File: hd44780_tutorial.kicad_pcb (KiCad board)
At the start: 2 copper layers, 157.2 x 83.5 mm, 33 parts, among them J1 LCD_2004_PinSocket_1x16_P2.54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, J2 UJC-HP-3-SMT-TR, SW1 REG SELECT, SW2 ENABLE, SW3 DS02C-254-1L-08BE

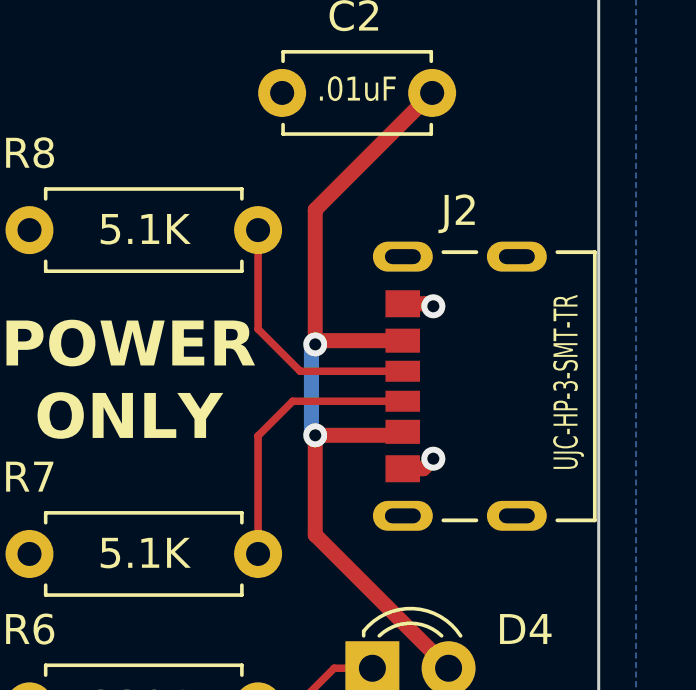
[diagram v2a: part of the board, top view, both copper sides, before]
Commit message: Moved footprint/model for USB-C connector to local library. Updated BOM. Updated images. Regenerated gerber/drill files.
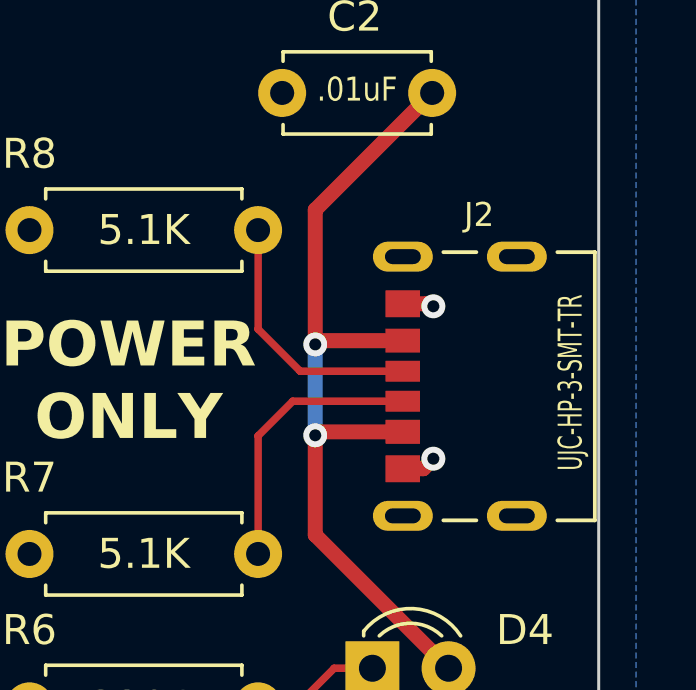
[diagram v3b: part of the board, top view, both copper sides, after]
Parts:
- J2: footprint Lutzcraft:CUI_UJC-HP-3-SMT-TR -> footprints:CUI_UJC-HP-3-SMT-TR
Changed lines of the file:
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@@
     )
   )
-  (footprint "Lutzcraft:CUI_UJC-HP-3-SMT-TR" (layer "F.Cu")
+  (footprint "footprints:CUI_UJC-HP-3-SMT-TR" (layer "F.Cu")
     (at 211.836 71.245 90)
     (property "MANUFACTURER" "CUI Devices")
@@
     (property "Sheetname" "")
     (attr smd)
-    (fp_text reference "J2" (at 5.84 1.895 180) (layer "F.SilkS")
-        (effects (font (size 1 1) (thickness 0.15)))
+    (fp_text reference "J2" (at 5.713 2.54 180) (layer "F.SilkS")
+        (effects (font (size 0.8 0.787402) (thickness 0.15)))
     )
-    (fp_text value "UJC-HP-3-SMT-TR" (at 0.125 5.451 90) (layer "F.SilkS")
-        (effects (font (size 0.8 0.5) (thickness 0.125)))
+    (fp_text value "UJC-HP-3-SMT-TR" (at 0.125 5.588 90) (layer "F.SilkS")
+        (effects (font (size 0.8 0.5) (thickness 0.1)))
     )
     (fp_line (start -4.47 2.45) (end -4.47 1.35)
@@
     (pad "S4" thru_hole oval (at 4.32 3.8 90) (size 1 2) (drill oval 0.5 1.2) (layers "*.Cu" "*.Mask")
       (net 30 "unconnected-(J2-SHIELD__3-PadS4)") (pinfunction "SHIELD__3") (pintype "passive+no_connect") (solder_mask_margin 0.102))
-    (model ":LUTZCRAFT_LIBS:3dmodels/UJC-HP-3-SMT-TR.step"
+    (model "${KIPRJMOD}/libraries/3dmodels/UJC-HP-3-SMT-TR.step"
       (offset (xyz 0 0 0))
       (scale (xyz 1 1 1))
@@
   (segment (start 208.915 69.85) (end 208.915 65.365) (width 0.5) (layer "F.Cu") (net 21))
   (segment (start 213.36 88.16) (end 207.54 93.98) (width 0.5) (layer "F.Cu") (net 21))
-  (segment (start 211.716 72.88) (end 211.831 72.765) (width 0.5) (layer "F.Cu") (net 21))
   (segment (start 164.084 50.8) (end 80.8482 50.8) (width 0.5) (layer "F.Cu") (net 21))
-  (segment (start 208.915 76.2) (end 213.36 80.645) (width 0.5) (layer "F.Cu") (net 21))
   (segment (start 112.4966 52.1716) (end 112.4966 50.8) (width 0.5) (layer "F.Cu") (net 21))
+  (segment (start 208.915 72.88) (end 208.915 76.2) (width 0.5) (layer "F.Cu") (net 21))
   (segment (start 208.915 65.365) (end 212.812 61.468) (width 0.5) (layer "F.Cu") (net 21))
   (segment (start 210.32 102.735) (end 208.32 104.735) (width 0.5) (layer "F.Cu") (net 21))
   (segment (start 209.04 69.725) (end 211.831 69.725) (width 0.5) (layer "F.Cu") (net 21))
-  (segment (start 208.915 72.88) (end 211.716 72.88) (width 0.5) (layer "F.Cu") (net 21))
   (segment (start 155.878 114.808) (end 159.31 118.24) (width 0.5) (layer "F.Cu") (net 21))
   (segment (start 210.32 100.2) (end 210.32 102.735) (width 0.5) (layer "F.Cu") (net 21))
+  (segment (start 209.03 72.765) (end 211.831 72.765) (width 0.5) (layer "F.Cu") (net 21))
   (segment (start 159.31 118.24) (end 165.81 118.24) (width 0.5) (layer "F.Cu") (net 21))
   (segment (start 112.4966 50.8) (end 112.4608 50.7642) (width 0.5) (layer "F.Cu") (net 21))
-  (segment (start 208.915 72.88) (end 208.915 76.2) (width 0.5) (layer "F.Cu") (net 21))
   (segment (start 124.46 114.855) (end 124.507 114.808) (width 0.5) (layer "F.Cu") (net 21))
+  (segment (start 208.915 76.2) (end 213.36 80.645) (width 0.5) (layer "F.Cu") (net 21))
   (segment (start 208.32 112.355) (end 208.32 105.2) (width 0.5) (layer "F.Cu") (net 21))
   (segment (start 210.32 97.036) (end 164.084 50.8) (width 0.5) (layer "F.Cu") (net 21))
@@
   (segment (start 80.8482 50.8) (end 79.4766 52.1716) (width 0.5) (layer "F.Cu") (net 21))
   (segment (start 210.32 100.2) (end 210.32 97.036) (width 0.5) (layer "F.Cu") (net 21))
+  (segment (start 208.915 72.88) (end 209.03 72.765) (width 0.5) (layer "F.Cu") (net 21))
   (segment (start 124.507 114.808) (end 155.878 114.808) (width 0.5) (layer "F.Cu") (net 21))
   (segment (start 208.32 104.735) (end 208.32 105.2) (width 0.5) (layer "F.Cu") (net 21))
   (via (at 208.915 72.88) (size 0.8) (drill 0.4) (layers "F.Cu" "B.Cu") (net 21))
   (via (at 208.915 69.85) (size 0.8) (drill 0.4) (layers "F.Cu" "B.Cu") (net 21))
-  (segment (start 208.915 69.85) (end 208.788 69.977) (width 0.5) (layer "B.Cu") (net 21))
-  (segment (start 208.788 72.753) (end 208.915 72.88) (width 0.5) (layer "B.Cu") (net 21))
-  (segment (start 208.788 69.977) (end 208.788 72.753) (width 0.5) (layer "B.Cu") (net 21))
+  (segment (start 208.915 72.88) (end 208.915 69.85) (width 0.5) (layer "B.Cu") (net 21))
   (segment (start 128.195 122.555) (end 134.695 122.555) (width 0.25) (layer "F.Cu") (net 22))
   (segment (start 88.317675 55.932675) (end 84.5566 52.1716) (width 0.25) (layer "F.Cu") (net 22))

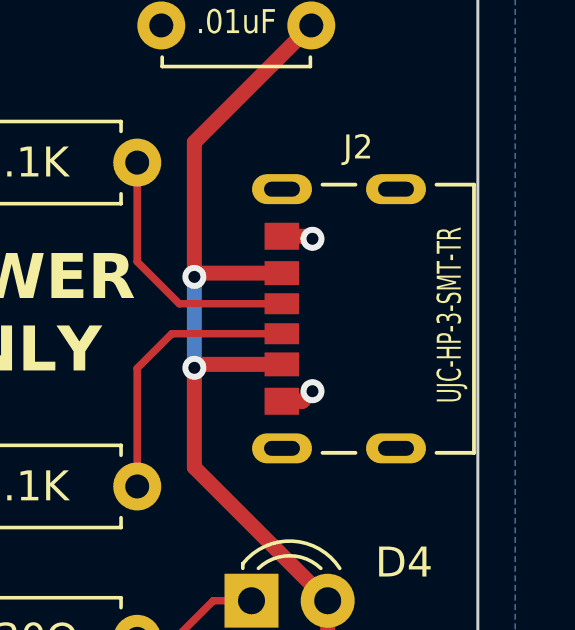
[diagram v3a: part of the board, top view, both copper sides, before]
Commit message: Change name and value of USB footprint to be correct.
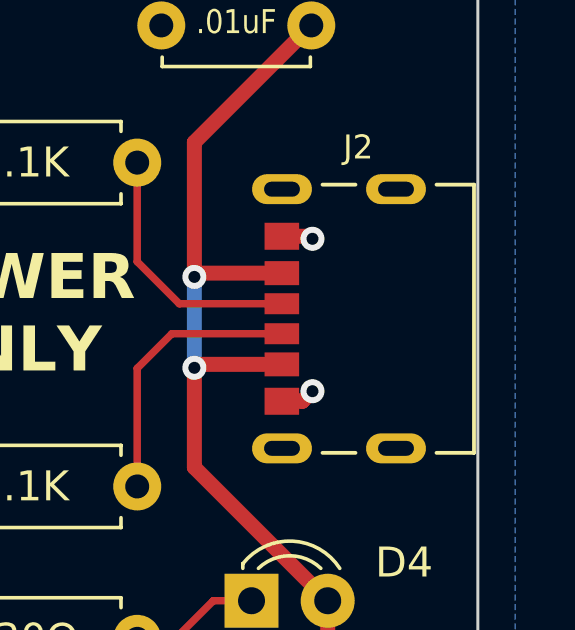
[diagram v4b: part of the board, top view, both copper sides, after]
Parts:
- J2: footprint footprints:CUI_UJC-HP-3-SMT-TR -> footprints:CUI_UJC-HP-M-G-5-MSMT-TR
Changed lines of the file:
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@@
     )
   )
-  (footprint "footprints:CUI_UJC-HP-3-SMT-TR" (layer "F.Cu")
+  (footprint "footprints:CUI_UJC-HP-M-G-5-MSMT-TR" (layer "F.Cu")
     (at 211.836 71.245 90)
     (property "MANUFACTURER" "CUI Devices")
@@
         (effects (font (size 0.8 0.787402) (thickness 0.15)))
     )
-    (fp_text value "UJC-HP-3-SMT-TR" (at 0.125 5.588 90) (layer "F.SilkS")
-        (effects (font (size 0.8 0.5) (thickness 0.1)))
+    (fp_text value "UJC-HP-3-SMT-TR" (at 1.524 -2 90) (layer "F.Fab")
+        (effects (font (size 0.787402 0.787402) (thickness 0.15)))
     )
     (fp_line (start -4.47 2.45) (end -4.47 1.35)
